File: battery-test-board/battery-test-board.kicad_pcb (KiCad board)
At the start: 2 copper layers, 118.9 x 134.4 mm, 58 parts, among them J1 Conn_02x04_Odd_Even, J10 Screw_Terminal_01x02, J2 Conn_02x04_Odd_Even, J3 Screw_Terminal_01x02, J4 Screw_Terminal_01x02, J5 Screw_Terminal_01x02, J6 Screw_Terminal_01x02, J7 Conn_02x04_Odd_Even, J8 Conn_02x20_Odd_Even, J9 Conn_02x20_Odd_Even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

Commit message: Updated footprints and PCB
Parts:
- added D1: diode, Diode_SMD:D_0805_2012Metric, F.Cu at (56.4, 28.6)
- added D10: diode, Diode_SMD:D_0805_2012Metric, F.Cu at (124.0, 28.4)
- added D15: Green, LED_SMD:LED_1206_3216Metric, F.Cu at (150.1, 122.5)
- added D16: Green, LED_SMD:LED_1206_3216Metric, F.Cu at (146.2, 122.5)
- added D2: diode, Diode_SMD:D_0805_2012Metric, F.Cu at (64.8, 139.1)
- added D4: diode, Diode_SMD:D_0805_2012Metric, F.Cu at (66.8, 139.1)
- added D5: diode, Diode_SMD:D_0805_2012Metric, F.Cu at (72.9, 28.7)
- added D7: diode, Diode_SMD:D_0805_2012Metric, F.Cu at (117.9, 138.9)
- added D8: diode, Diode_SMD:D_0805_2012Metric, F.Cu at (139.7, 28.4)
- added D9: diode, Diode_SMD:D_0805_2012Metric, F.Cu at (115.6, 138.9)
- added R17: 4k7, Resistor_SMD:R_1206_3216Metric, F.Cu at (150.1, 127.6)
- added R18: 10k, Resistor_SMD:R_1206_3216Metric, F.Cu at (146.2, 127.6)
- added REF**: MountingHole_3mm, MountingHole:MountingHole_3mm, F.Cu at (115.6, 122.3)
- added REF**: MountingHole_3mm, MountingHole:MountingHole_3mm, F.Cu at (30.7, 157.1)
- added REF**: MountingHole_3mm, MountingHole:MountingHole_3mm, F.Cu at (151.0, 28.7)
- added REF**: MountingHole_3mm, MountingHole:MountingHole_3mm, F.Cu at (64.8, 63.5)
- added REF**: MountingHole_3mm, MountingHole:MountingHole_3mm, F.Cu at (64.8, 122.3)
- added REF**: MountingHole_3mm, MountingHole:MountingHole_3mm, F.Cu at (151.0, 157.1)
- added REF**: MountingHole_3mm, MountingHole:MountingHole_3mm, F.Cu at (115.6, 63.5)
- added REF**: MountingHole_3mm, MountingHole:MountingHole_3mm, F.Cu at (30.7, 28.7)
- BT0, BT1, BT2, BT3: value BK-18650-PC2 -> battery
- C1, C2: value C -> 10u
- D11: renamed from D4; value D -> diode; footprint Diode_SMD:D_SOD-923 -> Diode_SMD:D_0805_2012Metric
- D12: renamed from D5; value D -> diode; footprint Diode_SMD:D_SOD-923 -> Diode_SMD:D_0805_2012Metric
- D13: renamed from D1; value LED -> Amber
- D14: renamed from D2; value LED -> Amber
- D3, D6: value D -> diode; footprint Diode_SMD:D_SOD-923 -> Diode_SMD:D_0805_2012Metric
- J8, J9: value Conn_02x20_Odd_Even -> connector; footprint Connector_PinSocket_2.54mm:PinSocket_2x20_P2.54mm_Vertical -> Connector_IDC:IDC-Header_2x20_P2.54mm_Vertical
- Q1, Q2: value PJA3412-AU_R1_000A1 -> mosfet
- R1, R3: value 330 -> 4k7
- R11, R5, R7, R9: value 1k -> 470
- U1, U10, U2, U3, U4, U5, U6, U7, U8, U9: value J104D2C12VDC.15S‎ -> relay
- moved D3 113.6 mm to (90.2, 28.6)
- moved D12 67.3 mm to (40.1, 34.7), turned to 180 degrees
- moved D6 50.8 mm to (107.4, 28.8)
- moved D11 26.7 mm to (37.8, 143.3)
- moved J8 3.67 mm to (31.9, 64.1)
- moved U4 3.05 mm to (65.4, 137.7)
- moved R16 2.43 mm to (140.7, 50.5), turned to -90 degrees
- moved U9 2.29 mm to (116.7, 137.8)
- moved J2 1.34 mm to (31.8, 56.6)
- moved J1 1.14 mm to (31.9, 128.5)
- moved BT1 1.02 mm to (78.5, 56.5)
- moved BT2 1.02 mm to (101.9, 56.5)
- moved BT0 1.02 mm to (51.1, 56.5)
- moved BT3 1.02 mm to (129.3, 56.5)
- moved J7 0.99 mm to (148.0, 49.0)
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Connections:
- D3 pad 2: relay_c -> relay_v
- J8 pad 11: batt_2+ -> batt_2-
- J8 pad 12: batt_2- -> batt_2+
- J8 pad 15: batt_3+ -> batt_3-
- J8 pad 16: batt_3- -> batt_3+
- J8 pad 19: batt_0t -> batt_1t
- J8 pad 20: batt_1t -> batt_0t
- J8 pad 23: batt_2t -> batt_3t
- J8 pad 24: batt_3t -> batt_2t
- J8 pad 29: bank_0c -> bank_0m
- J8 pad 3: batt_0+ -> batt_0-
- J8 pad 30: bank_0m -> bank_0c
- J8 pad 31: bank_1c -> bank_1m
- J8 pad 32: bank_1m -> bank_1c
- J8 pad 33: bank_2c -> bank_2m
- J8 pad 34: bank_2m -> bank_2c
- J8 pad 35: bank_3c -> bank_3m
- J8 pad 36: bank_3m -> bank_3c
- J8 pad 4: batt_0- -> batt_0+
- J8 pad 7: batt_1+ -> batt_1-
- J8 pad 8: batt_1- -> batt_1+
- J9 pad 11: batt_2+ -> batt_2-
- J9 pad 12: batt_2- -> batt_2+
- J9 pad 15: batt_3+ -> batt_3-
- J9 pad 16: batt_3- -> batt_3+
- J9 pad 19: batt_0t -> batt_1t
- J9 pad 20: batt_1t -> batt_0t
- J9 pad 23: batt_2t -> batt_3t
- J9 pad 24: batt_3t -> batt_2t
- J9 pad 29: bank_0c -> bank_0m
- J9 pad 3: batt_0+ -> batt_0-
- J9 pad 30: bank_0m -> bank_0c
- J9 pad 31: bank_1c -> bank_1m
- J9 pad 32: bank_1m -> bank_1c
- J9 pad 33: bank_2c -> bank_2m
- J9 pad 34: bank_2m -> bank_2c
- J9 pad 35: bank_3c -> bank_3m
- J9 pad 36: bank_3m -> bank_3c
- J9 pad 4: batt_0- -> batt_0+
- J9 pad 7: batt_1+ -> batt_1-
- J9 pad 8: batt_1- -> batt_1+
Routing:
- net +12V: track 303.3 -> 372.9 mm
- net +5V: track 126.6 -> 138.4 mm
- net batt_2-: track 156.2 -> 162.7 mm
- net batt_1-: track 151.4 -> 157.6 mm
- net batt_0-: track 151.6 -> 157.8 mm
- net bank_0c: track 142.7 -> 148.0 mm
- net bank_3m: track 165.4 -> 170.5 mm
- net bank_1m: track 167.1 -> 172.2 mm
- net bank_2m: track 166.4 -> 171.5 mm
- net bank_2c: track 133.0 -> 138.1 mm
- net bank_1c: track 138.5 -> 143.6 mm
- net bank_3c: track 127.5 -> 132.6 mm
- net bank_0m: track 168.0 -> 172.7 mm
- net batt_3t: track 168.3 -> 172.0 mm
- net batt_1t: track 162.4 -> 166.1 mm
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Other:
- board size 118.9 x 134.4 mm -> 126.1 x 134.2 mm
- board text added: "12V@200mA Relay Power"
- board text added: "Battery Tester V1.0 03/28/22"
- board text added: "Designed by Benjamin Crall for PSAS"
- board text added: "Jump each row on J7 on only one board"
- board text added: "TODO fix spacing between pads"
- board text removed: "Battery Test V1.0"
- board text removed: "Jump each row on J7 on only 1 board"

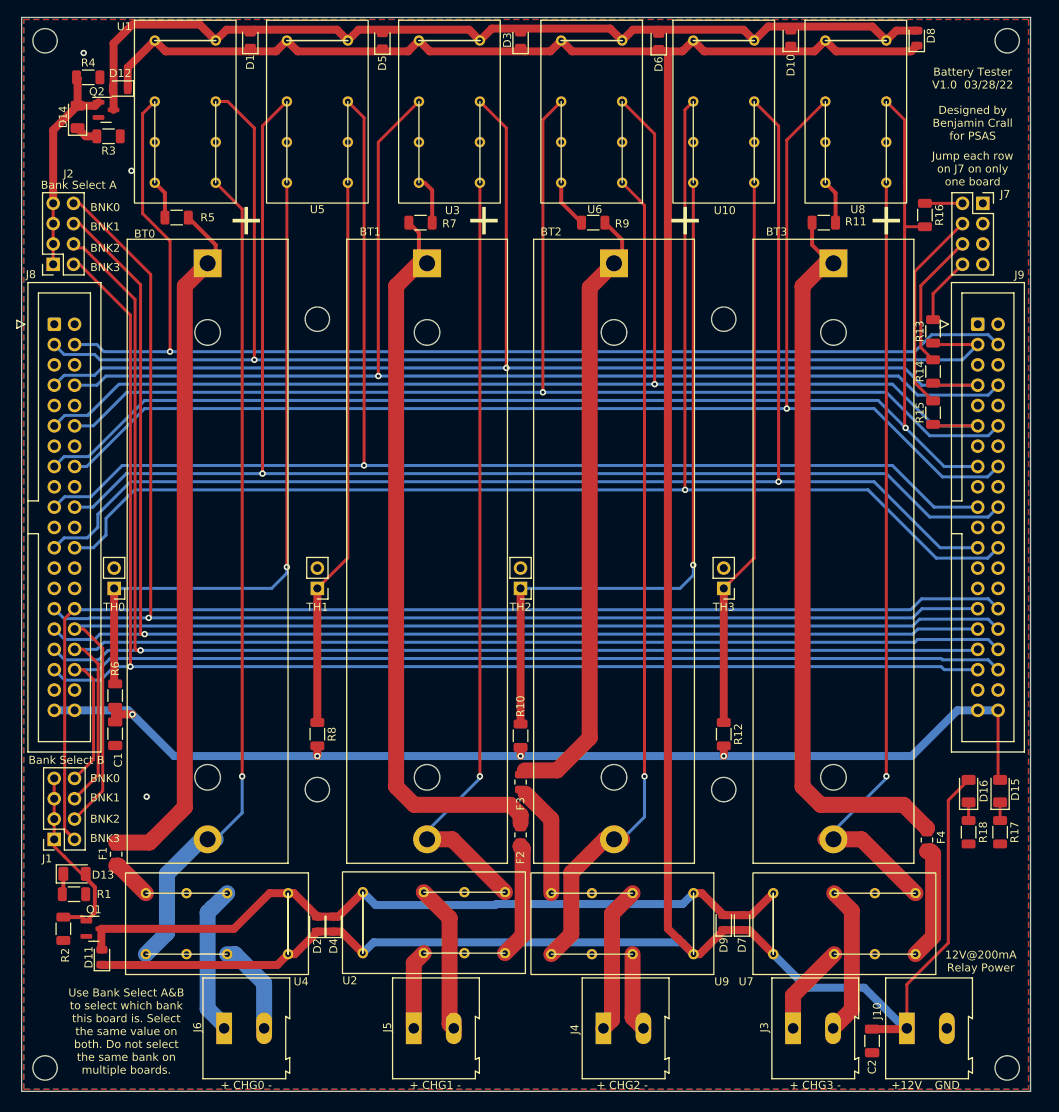
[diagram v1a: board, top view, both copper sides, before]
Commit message: Fixed silk screen and a few other things
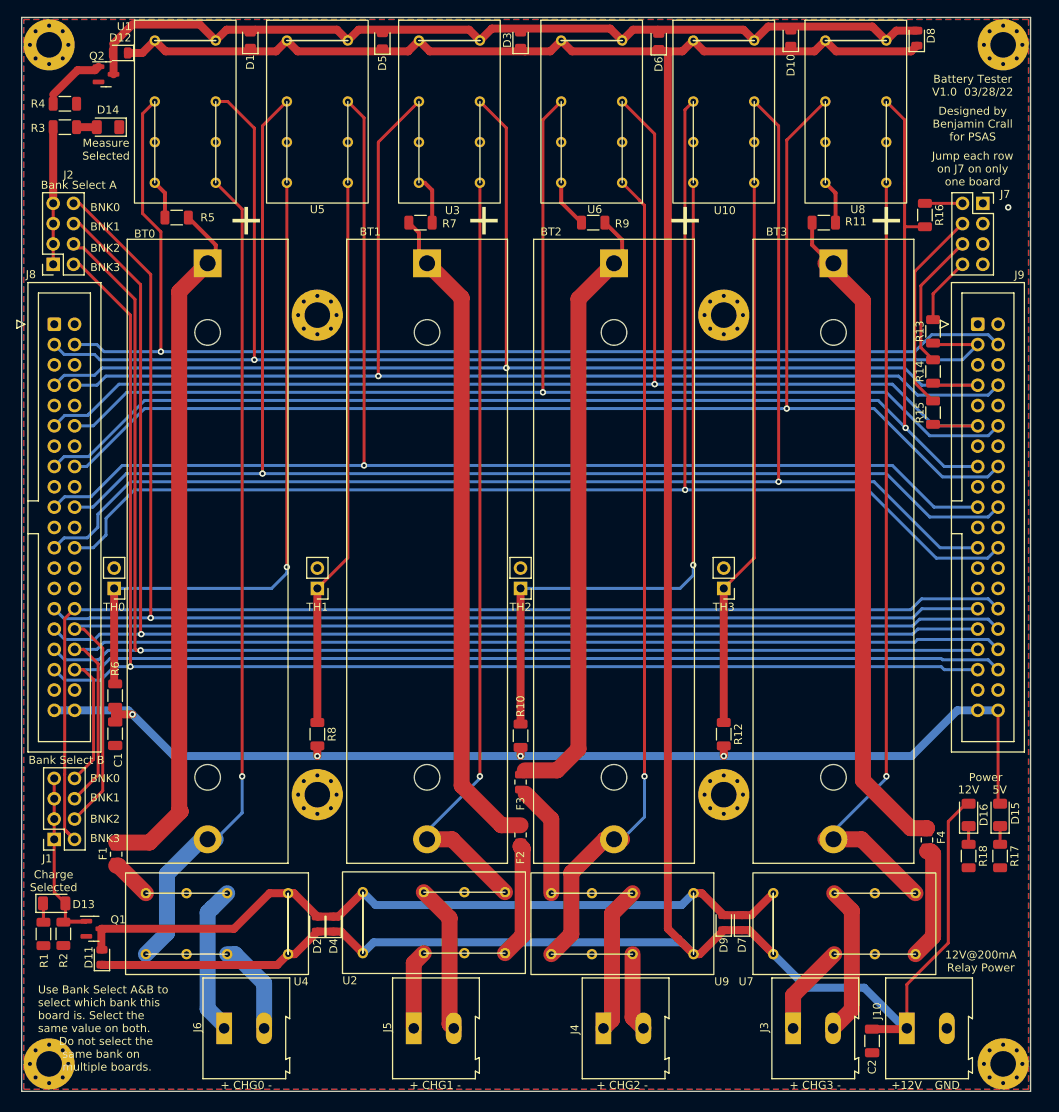
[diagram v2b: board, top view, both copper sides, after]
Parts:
- removed REF** (x8): MountingHole_3mm, MountingHole:MountingHole_3mm
- added H1: MountingHole_3.2mm_M3_Pad_Via, MountingHole:MountingHole_3.2mm_M3_Pad_Via, F.Cu at (31.2, 29.2)
- added H2: MountingHole_3.2mm_M3_Pad_Via, MountingHole:MountingHole_3.2mm_M3_Pad_Via, F.Cu at (150.5, 29.2)
- added H3: MountingHole_3.2mm_M3_Pad_Via, MountingHole:MountingHole_3.2mm_M3_Pad_Via, F.Cu at (64.8, 63.0)
- added H4: MountingHole_3.2mm_M3_Pad_Via, MountingHole:MountingHole_3.2mm_M3_Pad_Via, F.Cu at (115.6, 63.0)
- added H5: MountingHole_3.2mm_M3_Pad_Via, MountingHole:MountingHole_3.2mm_M3_Pad_Via, F.Cu at (64.8, 122.9)
- added H6: MountingHole_3.2mm_M3_Pad_Via, MountingHole:MountingHole_3.2mm_M3_Pad_Via, F.Cu at (115.6, 122.9)
- added H7: MountingHole_3.2mm_M3_Pad_Via, MountingHole:MountingHole_3.2mm_M3_Pad_Via, F.Cu at (31.2, 156.6)
- added H8: MountingHole_3.2mm_M3_Pad_Via, MountingHole:MountingHole_3.2mm_M3_Pad_Via, F.Cu at (150.5, 156.6)
- moved R1 6.27 mm to (30.5, 140.3), turned to 90 degrees
- moved R3 5.58 mm to (33.2, 39.5), turned to 0 degrees
- moved D13 4.48 mm to (31.9, 136.5)
- moved D12 4.45 mm to (40.1, 30.2)
- moved Q2 4.45 mm to (38.4, 32.9)
- moved R4 4.41 mm to (33.2, 36.6)
- moved D14 4.01 mm to (38.6, 39.5), turned to 180 degrees
- moved D15 2.97 mm to (150.1, 125.5)
- moved D16 2.97 mm to (146.2, 125.5)
- moved R17 2.97 mm to (150.1, 130.6)
- moved R18 2.97 mm to (146.2, 130.6)
- moved R2 0.64 mm to (33.0, 140.3)
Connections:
- D14 pad 1: Net-(D14-Pad1) -> GND
- D14 pad 2: Net-(D14-Pad2) -> Net-(R3-Pad2)
- J2 pad 1: Net-(D14-Pad2) -> Net-(J2-Pad1)
- J2 pad 3: Net-(D14-Pad2) -> Net-(J2-Pad1)
- J2 pad 5: Net-(D14-Pad2) -> Net-(J2-Pad1)
- J2 pad 7: Net-(D14-Pad2) -> Net-(J2-Pad1)
- Q2 pad 1: Net-(D14-Pad2) -> Net-(J2-Pad1)
- R3 pad 1: GND -> Net-(J2-Pad1)
- R3 pad 2: Net-(D14-Pad1) -> Net-(R3-Pad2)
- R4 pad 1: Net-(D14-Pad2) -> Net-(J2-Pad1)
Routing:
- net Net-(D14-Pad2): track 27.5 -> 0.00 mm
- net Net-(J2-Pad1): track 0.00 -> 23.9 mm
- net Net-(BT1-Pad1): track 90.3 -> 82.1 mm
- net Net-(BT3-Pad1): track 90.1 -> 82.8 mm
- net +12V: track 372.9 -> 366.8 mm
- net relay_v: track 117.2 -> 112.8 mm
- net +5V: track 138.4 -> 141.3 mm
- net Net-(D13-Pad2): track 23.8 -> 21.0 mm
- net Net-(D14-Pad1): track 2.83 -> 0.00 mm
- net Net-(R3-Pad2): track 0.00 -> 2.54 mm
- net GND: vias 3 -> 1
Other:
- board text added: "12V"
- board text added: "5V"
- board text added: "Charge Selected"
- board text added: "Measure Selected"
- board text added: "Power"

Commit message: Finished BOM
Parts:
- F1, F2, F3, F4: footprint Fuse:Fuse_0805_2012Metric -> Fuse:Fuse_2920_7451Metric
- R18: value 10k -> 10K
- moved F2 27.1 mm to (64.8, 118.4)
- moved F3 25.6 mm to (115.6, 118.6)
- moved R10 6.17 mm to (90.2, 109.4)
- moved R8 5.98 mm to (64.7, 109.4)
- moved R12 5.98 mm to (115.6, 109.4)
- moved F1 5.82 mm to (37.3, 135.7)
- moved H5 4.56 mm to (64.8, 127.5)
- moved H6 4.56 mm to (115.6, 127.5)
- moved Q1 2.50 mm to (36.7, 142.2)
- moved F4 2.50 mm to (142.9, 127.0)
- moved D15 1.88 mm to (151.8, 126.2)
- moved D16 1.88 mm to (147.9, 126.2)
- moved R17 1.88 mm to (151.8, 131.4)
- moved R18 1.88 mm to (147.9, 131.4)
- moved D11 1.86 mm to (39.7, 143.4)
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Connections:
- U7 pad 13: charge_2- -> charge_2+
- U7 pad 4: charge_2+ -> charge_2-
- U7 pad 8: Net-(F3-Pad2) -> Net-(BT2-Pad2)
- U7 pad 9: Net-(BT2-Pad2) -> Net-(F3-Pad2)
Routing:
- net Net-(F2-Pad2): track 14.4 -> 42.9 mm
- net Net-(F3-Pad2): track 13.8 -> 33.4 mm
- net Net-(BT1-Pad1): track 82.1 -> 73.4 mm
- net charge_2-: track 9.83 -> 18.4 mm
- net Net-(BT2-Pad2): track 103.7 -> 96.2 mm
- net charge_2+: track 18.4 -> 11.0 mm
- net Net-(R10-Pad2): track 88.3 -> 82.1 mm
- net Net-(R12-Pad1): track 69.0 -> 63.1 mm
- net Net-(R8-Pad1): track 69.0 -> 63.1 mm
- net Net-(BT2-Pad1): track 76.4 -> 81.5 mm
- net Net-(J2-Pad1): track 23.9 -> 28.0 mm
- net +12V: track 366.8 -> 364.3 mm
- net GND: track 0.36 -> 2.85 mm
- net Net-(F1-Pad2): track 5.14 -> 7.63 mm
- net Net-(D13-Pad2): track 21.0 -> 23.4 mm
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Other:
- board text added: "Battery Tester V1.0 03/30/22"
- board text removed: "Battery Tester V1.0 03/28/22"

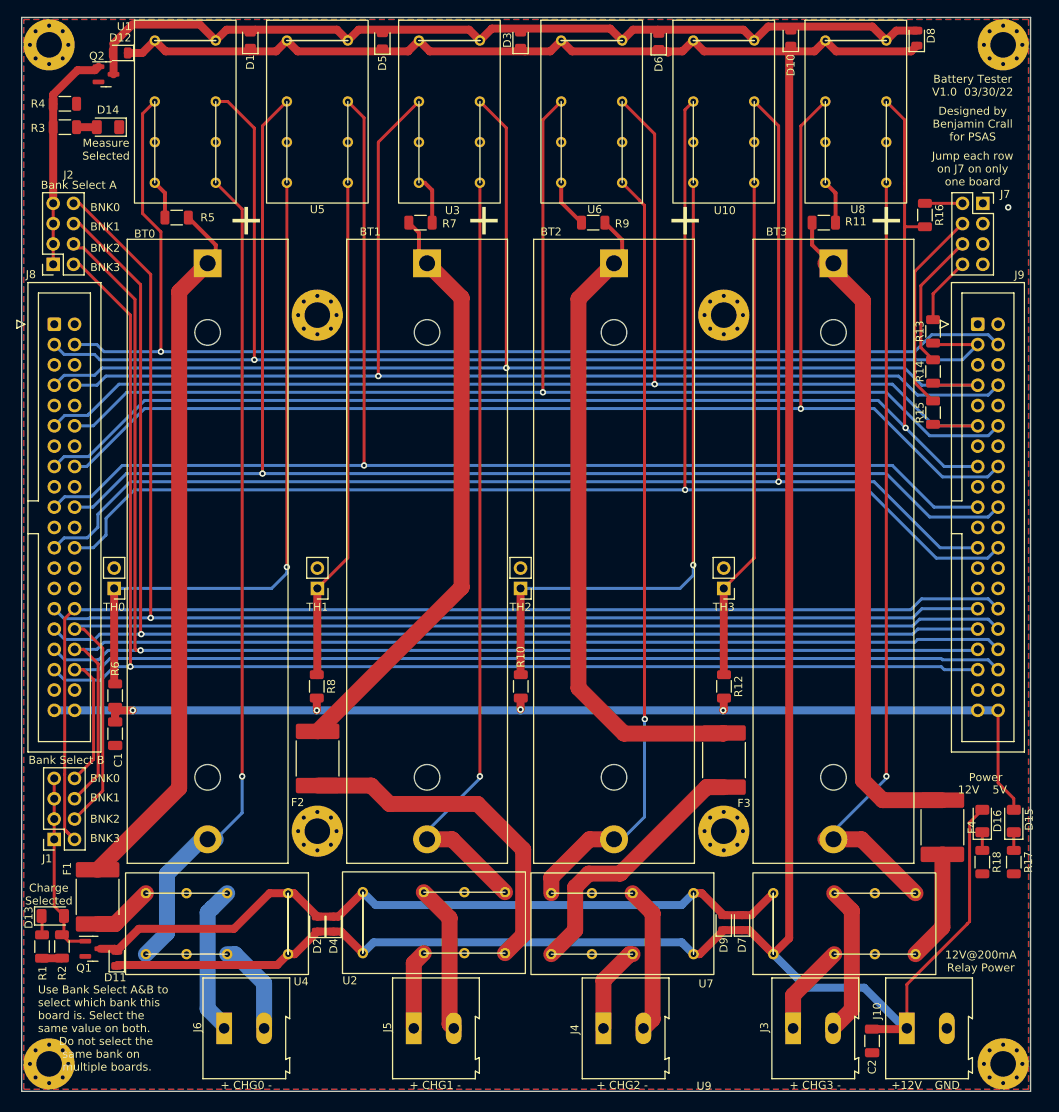
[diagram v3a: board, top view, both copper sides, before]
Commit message: Changed silkscreen
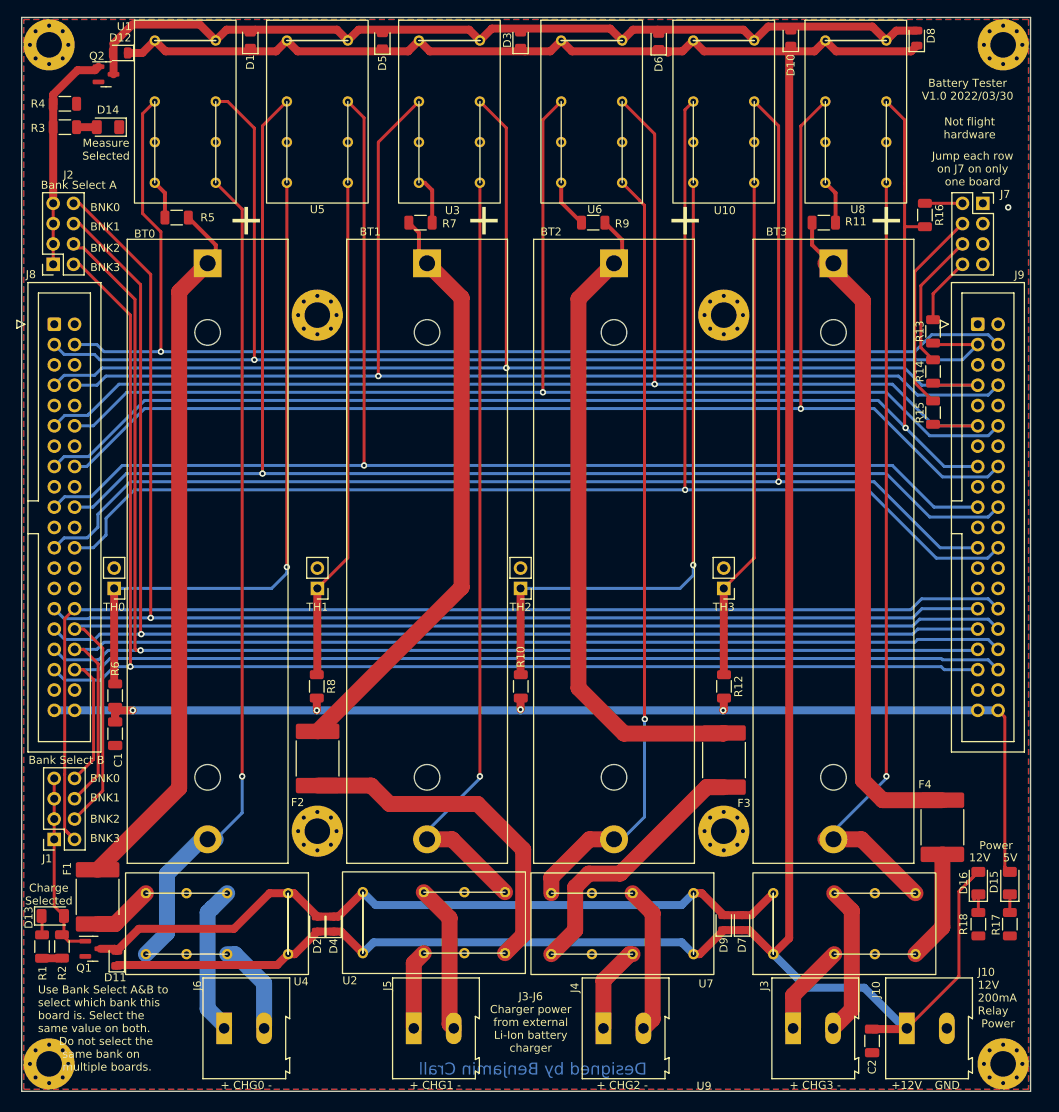
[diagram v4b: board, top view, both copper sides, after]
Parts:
- moved R17 7.78 mm to (151.3, 139.1)
- moved R18 7.78 mm to (147.4, 139.1)
- moved D15 7.78 mm to (151.3, 134.0)
- moved D16 7.78 mm to (147.4, 134.0)
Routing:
- net +5V: track 139.1 -> 146.7 mm
- net +12V: track 364.3 -> 358.6 mm
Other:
- board text added: "Battery Tester V1.0 2022/03/30"
- board text added: "Designed by Benjamin Crall"
- board text added: "J10 12V 200mA Relay Power"
- board text added: "J3-J6 Charger power from external Li-Ion battery charger"
- board text added: "Not flight hardware"
- board text removed: "12V@200mA Relay Power"
- board text removed: "Battery Tester V1.0 03/30/22"
- board text removed: "Designed by Benjamin Crall for PSAS"
- board text removed: "TODO fix spacing between pads"

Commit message: Added sticker
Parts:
- added REF**: logo-small, oresat-logo:logo-small, F.Cu at (67.8, 152.1)
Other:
- board text removed: "Not flight hardware"

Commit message: Made stuff prettier
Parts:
- moved R5 1.48 mm to (48.3, 51.8)
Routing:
- net Net-(BT2-Pad1): track 81.5 -> 75.8 mm
- net Net-(BT1-Pad1): track 73.4 -> 69.8 mm
- net Net-(BT0-Pad2): track 104.3 -> 102.3 mm
- net Net-(R5-Pad2): track 4.88 -> 6.34 mm
- net Net-(BT0-Pad1): track 88.6 -> 87.2 mm
- net Net-(BT3-Pad2): track 99.3 -> 98.3 mm
- net Net-(BT2-Pad2): track 96.2 -> 97.2 mm
